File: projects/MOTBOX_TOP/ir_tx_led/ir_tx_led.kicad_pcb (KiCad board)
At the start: 2 copper layers, 8 x 8 mm, 2 parts, among them J1 Conn_01x02

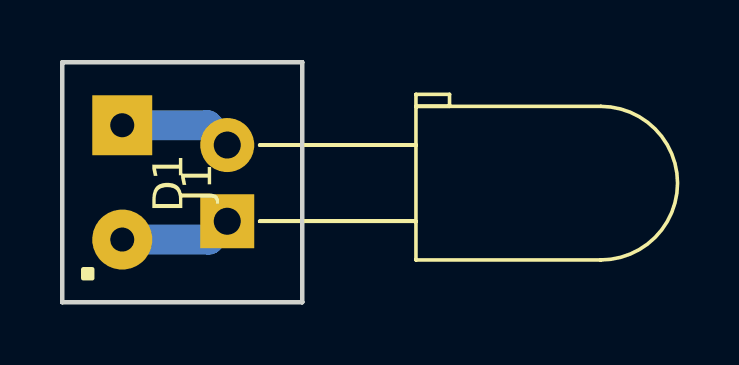
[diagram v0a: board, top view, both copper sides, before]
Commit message: New library files and schematics with ESE31 and DT045 switches
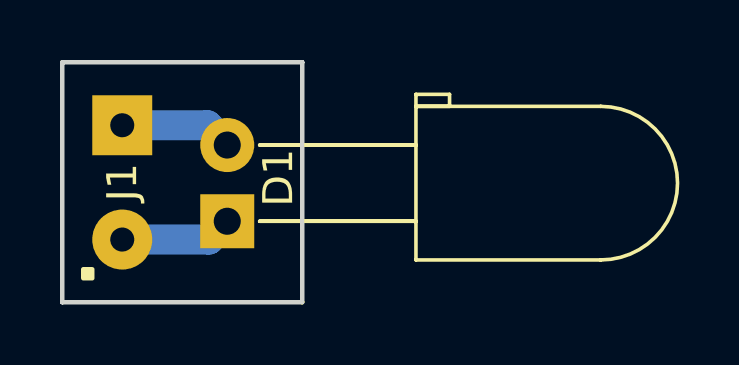
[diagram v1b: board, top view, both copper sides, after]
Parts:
- D1: value LED -> IR333-A
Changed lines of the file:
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@@
     (solder_mask_min_width 0.25)
     (aux_axis_origin 0 0)
-    (visible_elements FFF9FF7F)
+    (visible_elements FFFDFF7F)
     (pcbplotparams
-      (layerselection 0x010fc_ffffffff)
-      (usegerberextensions false)
+      (layerselection 0x010fc_fffffffe)
+      (usegerberextensions true)
       (usegerberattributes false)
       (usegerberadvancedattributes false)
@@
       (outputformat 1)
       (mirror false)
-      (drillshape 1)
+      (drillshape 0)
       (scaleselection 1)
-      (outputdirectory ""))
+      (outputdirectory "Gerber/"))
   )
   (net 0 "")
@@
     (descr "LED, diameter 5.0mm z-position of LED center 3.0mm, 2 pins, diameter 5.0mm z-position of LED center 3.0mm, 2 pins, diameter 5.0mm z-position of LED center 3.0mm, 2 pins, diameter 5.0mm z-position of LED center 9.0mm, 2 pins, diameter 5.0mm z-position of LED center 9.0mm, 2 pins, diameter 5.0mm z-position of LED center 9.0mm, 2 pins")
     (tags "LED diameter 5.0mm z-position of LED center 3.0mm 2 pins diameter 5.0mm z-position of LED center 3.0mm 2 pins diameter 5.0mm z-position of LED center 3.0mm 2 pins diameter 5.0mm z-position of LED center 9.0mm 2 pins diameter 5.0mm z-position of LED center 9.0mm 2 pins diameter 5.0mm z-position of LED center 9.0mm 2 pins")
-    (fp_text reference D1 (at 1.27 -1.96 90) (layer F.SilkS)
+    (fp_text reference D1 (at 1.45 1.7 90) (layer F.SilkS)
       (effects (font (size 1 1) (thickness 0.15)))
     )
-    (fp_text value LED (at 1.27 16.01 90) (layer F.Fab)
+    (fp_text value IR333-A (at 1.27 16.01 90) (layer F.Fab)
       (effects (font (size 1 1) (thickness 0.15)))
     )
@@
     (tags connector)
     (attr virtual)
-    (fp_text reference J1 (at 1.905 -2.5 270) (layer F.SilkS)
+    (fp_text reference J1 (at 1.9 0 270) (layer F.SilkS)
       (effects (font (size 1 1) (thickness 0.15)))
     )
